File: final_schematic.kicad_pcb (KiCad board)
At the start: 2 copper layers, 54.7 x 60.6 mm, 56 parts, among them J1 Battery Babysitter, J2 BB_SYSOFF, J4 OLED Qwiic, J5 Programmer, J8 GPS_COAX, SW1 SW_Push_SESS, SW2 SW_Push_RADIO, SW3 SW_Push_RST, U1 STM32L476VGTx, U2 MTK3339, U3 RFM95W-868S2, U4 BNO055, U5 LT1129-3.3_SO8, U6 TC2014-3.3VxCTTR

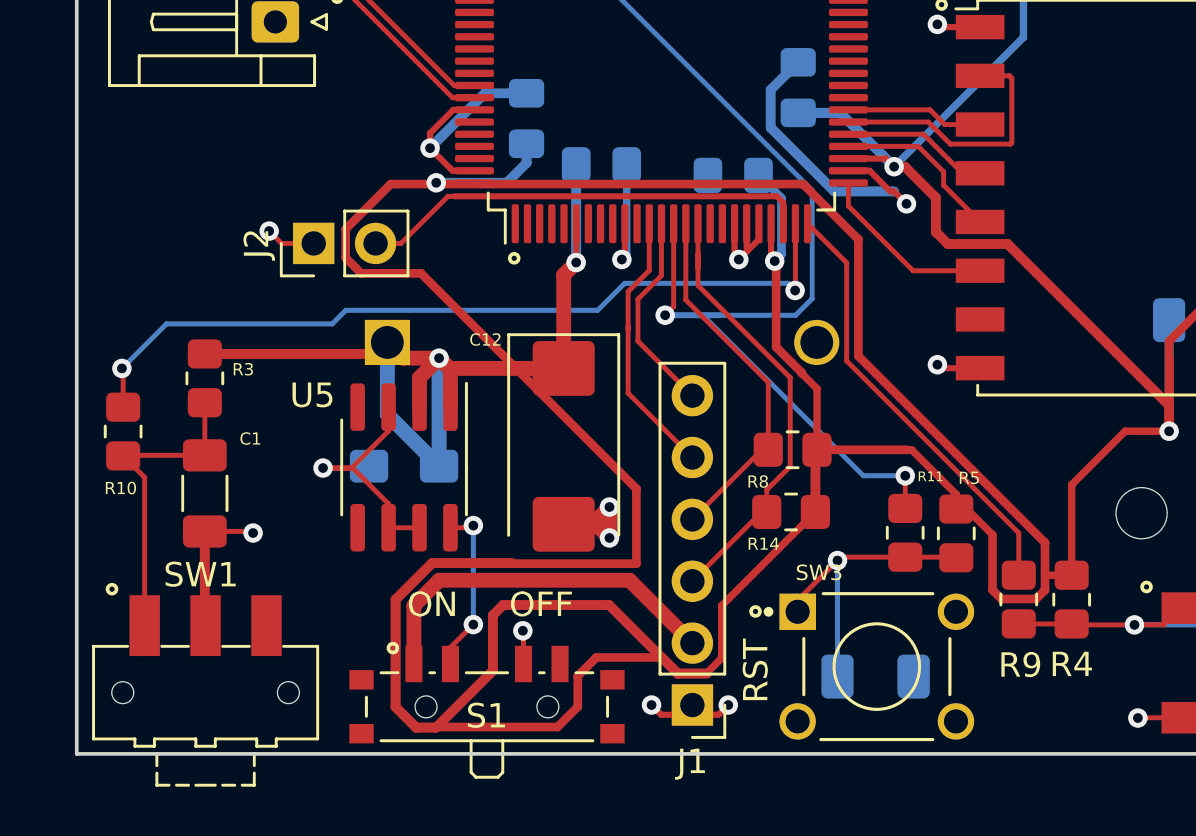
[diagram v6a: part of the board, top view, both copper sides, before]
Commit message: routing minimization
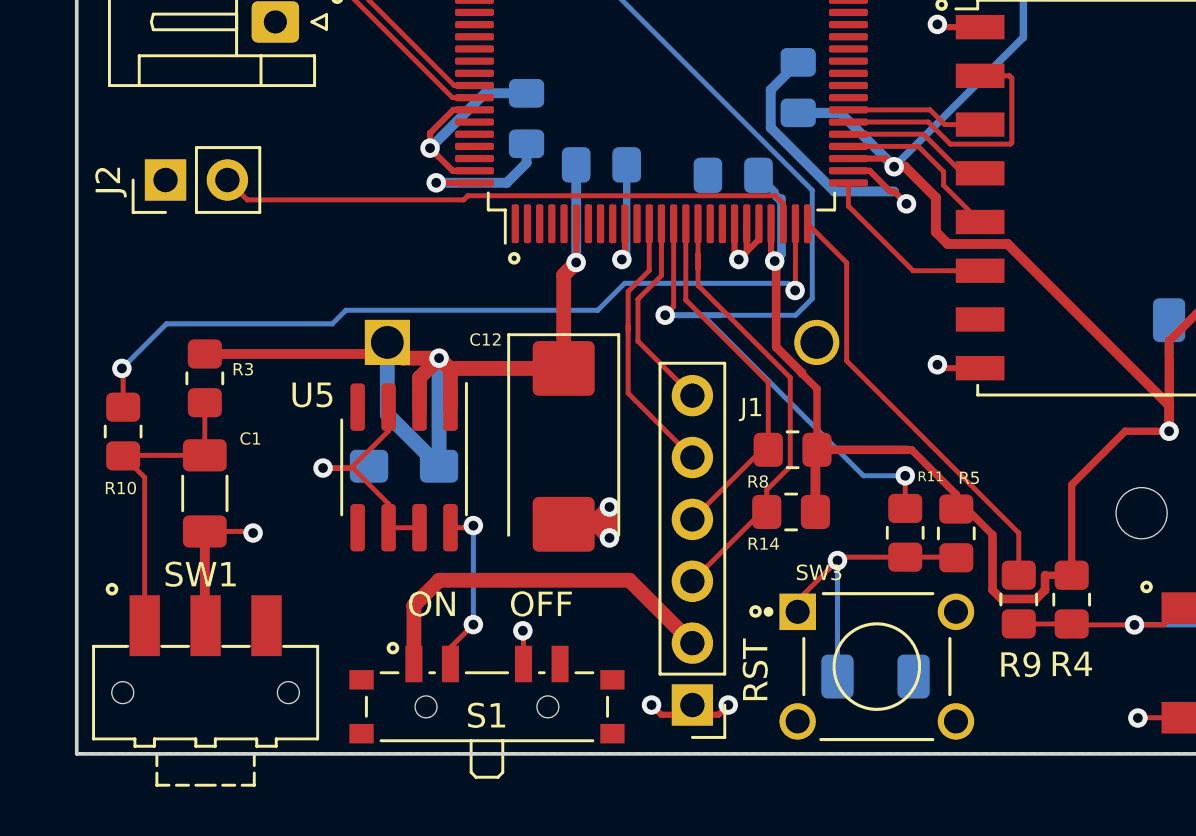
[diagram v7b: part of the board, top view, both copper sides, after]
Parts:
- moved J2 6.62 mm to (100.9, 82.3)
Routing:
- net 3V3: track 370.4 -> 244.5 mm
- net SYSOFF: track 18.5 -> 24.2 mm
- net GND: track 150.0 -> 148.0 mm, vias 27 -> 26
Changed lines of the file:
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@@
     (thickness 1.6)
     (drawings 51)
-    (tracks 612)
+    (tracks 573)
     (zones 0)
     (modules 56)
@@
   )
   (setup
-    (last_trace_width 0.254)
+    (last_trace_width 0.2032)
     (user_trace_width 0.2032)
     (user_trace_width 0.254)
@@
     )
   )
-  (module Connector_PinHeader_2.54mm:PinHeader_1x02_P2.54mm_Vertical (layer F.Cu)
-    (at 106.9848 84.9376 90)
+  (module Connector_PinHeader_2.54mm:PinHeader_1x02_P2.54mm_Vertical locked (layer F.Cu)
+    (at 100.9015 82.3341 90)
     (descr "Through hole straight pin header, 1x02, 2.54mm pitch, single row")
     (tags "Through hole pin header THT 1x02 2.54mm single row")
@@
     )
   )
-  (module Connector_PinHeader_2.54mm:PinHeader_1x06_P2.54mm_Vertical (layer F.Cu)
+  (module Connector_PinHeader_2.54mm:PinHeader_1x06_P2.54mm_Vertical locked (layer F.Cu)
     (at 122.5296 103.886 180)
     (descr "Through hole straight pin header, 1x06, 2.54mm pitch, single row")
     (tags "Through hole pin header THT 1x06 2.54mm single row")
-    (fp_text reference J1 (at 0 -2.33) (layer F.SilkS)
-      (effects (font (size 1 1) (thickness 0.15)))
+    (fp_text reference J1 (at -2.4384 12.2047) (layer F.SilkS)
+      (effects (font (size 0.75 0.75) (thickness 0.15)))
     )
     (fp_text value "Battery Babysitter" (at 0 15.03) (layer F.Fab)
@@
   (segment (start 130.468 70.954) (end 130.4925 70.9295) (width 0.254) (layer F.Cu) (net 2))
   (segment (start 128.9346 70.954) (end 130.468 70.954) (width 0.254) (layer F.Cu) (net 2))
-  (via (at 105.156 84.4296) (size 0.8) (drill 0.4) (layers F.Cu B.Cu) (net 2))
-  (segment (start 105.664 84.9376) (end 105.156 84.4296) (width 0.2032) (layer F.Cu) (net 2))
-  (segment (start 106.9848 84.9376) (end 105.664 84.9376) (width 0.2032) (layer F.Cu) (net 2))
   (segment (start 122.153494 103.4956) (end 122.5296 103.4956) (width 0.6096) (layer F.Cu) (net 2))
   (segment (start 107.556399 61.201399) (end 107.895224 61.201399) (width 0.2032) (layer F.Cu) (net 24))
@@
   (segment (start 127.5809 93.472) (end 127.6444 93.4085) (width 0.4064) (layer F.Cu) (net 5))
   (segment (start 127.5809 95.9612) (end 127.5809 93.472) (width 0.4064) (layer F.Cu) (net 5))
-  (segment (start 110.343599 99.558418) (end 111.845228 98.056789) (width 0.4064) (layer F.Cu) (net 5))
-  (segment (start 111.845228 98.056789) (end 115.125771 98.056789) (width 0.4064) (layer F.Cu) (net 5))
-  (segment (start 114.758865 99.780799) (end 114.341201 100.198463) (width 0.4064) (layer F.Cu) (net 5))
-  (segment (start 112.006337 104.815201) (end 111.187263 104.815201) (width 0.4064) (layer F.Cu) (net 5))
-  (segment (start 123.131137 102.599201) (end 121.928063 102.599201) (width 0.4064) (layer F.Cu) (net 5))
-  (segment (start 121.928063 102.599201) (end 119.109661 99.780799) (width 0.4064) (layer F.Cu) (net 5))
-  (segment (start 114.341201 100.198463) (end 114.341201 102.480337) (width 0.4064) (layer F.Cu) (net 5))
-  (segment (start 110.343599 103.971537) (end 110.343599 99.558418) (width 0.4064) (layer F.Cu) (net 5))
-  (segment (start 114.341201 102.480337) (end 112.006337 104.815201) (width 0.4064) (layer F.Cu) (net 5))
-  (segment (start 119.109661 99.780799) (end 114.758865 99.780799) (width 0.4064) (layer F.Cu) (net 5))
-  (segment (start 111.187263 104.815201) (end 110.343599 103.971537) (width 0.4064) (layer F.Cu) (net 5))
-  (segment (start 121.940255 102.573801) (end 123.118945 102.573801) (width 0.3556) (layer F.Cu) (net 5))
-  (segment (start 121.301799 101.935345) (end 121.940255 102.573801) (width 0.3556) (layer F.Cu) (net 5))
-  (segment (start 118.583413 101.935345) (end 121.301799 101.935345) (width 0.3556) (layer F.Cu) (net 5))
-  (segment (start 117.824601 102.694157) (end 118.583413 101.935345) (width 0.3556) (layer F.Cu) (net 5))
-  (segment (start 117.824601 103.959345) (end 117.824601 102.694157) (width 0.3556) (layer F.Cu) (net 5))
-  (segment (start 116.994145 104.789801) (end 117.824601 103.959345) (width 0.3556) (layer F.Cu) (net 5))
-  (segment (start 111.199455 104.789801) (end 116.994145 104.789801) (width 0.3556) (layer F.Cu) (net 5))
-  (segment (start 110.368999 103.959345) (end 111.199455 104.789801) (width 0.3556) (layer F.Cu) (net 5))
-  (segment (start 110.368999 99.568939) (end 110.368999 103.959345) (width 0.3556) (layer F.Cu) (net 5))
-  (segment (start 111.855748 98.08219) (end 110.368999 99.568939) (width 0.3556) (layer F.Cu) (net 5))
-  (segment (start 120.231145 98.082189) (end 111.855748 98.08219) (width 0.3556) (layer F.Cu) (net 5))
-  (segment (start 120.231145 95.005489) (end 120.231145 98.082189) (width 0.3556) (layer F.Cu) (net 5))
-  (segment (start 111.391057 86.165401) (end 120.231145 95.005489) (width 0.3556) (layer F.Cu) (net 5))
-  (segment (start 108.935455 86.165401) (end 111.391057 86.165401) (width 0.3556) (layer F.Cu) (net 5))
-  (segment (start 108.296999 85.526945) (end 108.935455 86.165401) (width 0.3556) (layer F.Cu) (net 5))
-  (segment (start 108.296999 84.348255) (end 108.296999 85.526945) (width 0.3556) (layer F.Cu) (net 5))
-  (segment (start 110.144074 82.50118) (end 108.296999 84.348255) (width 0.3556) (layer F.Cu) (net 5))
-  (segment (start 127.072152 82.50118) (end 110.144074 82.50118) (width 0.3556) (layer F.Cu) (net 5))
-  (segment (start 129.343111 84.772139) (end 127.072152 82.50118) (width 0.3556) (layer F.Cu) (net 5))
-  (segment (start 129.343111 89.563125) (end 129.343111 84.772139) (width 0.3556) (layer F.Cu) (net 5))
-  (segment (start 137.00591 97.225924) (end 129.343111 89.563125) (width 0.3556) (layer F.Cu) (net 5))
   (segment (start 136.63815 99.53311) (end 137.00591 99.16535) (width 0.3556) (layer F.Cu) (net 5))
   (segment (start 135.21805 99.53311) (end 136.63815 99.53311) (width 0.3556) (layer F.Cu) (net 5))
@@
   (segment (start 127.6444 90.903262) (end 127.6444 93.4085) (width 0.3048) (layer F.Cu) (net 5))
   (segment (start 127.025419 90.284281) (end 127.6444 90.903262) (width 0.3048) (layer F.Cu) (net 5))
-  (segment (start 123.732001 99.810099) (end 127.5809 95.9612) (width 0.3048) (layer F.Cu) (net 5))
-  (segment (start 123.732001 101.960745) (end 123.732001 99.810099) (width 0.3048) (layer F.Cu) (net 5))
-  (segment (start 123.118945 102.573801) (end 123.732001 101.960745) (width 0.3048) (layer F.Cu) (net 5))
   (segment (start 133.795652 95.8408) (end 134.85029 96.895438) (width 0.3048) (layer F.Cu) (net 5))
   (segment (start 133.3627 95.8408) (end 133.795652 95.8408) (width 0.3048) (layer F.Cu) (net 5))
@@
   (segment (start 137.0142 98.5586) (end 137.00591 98.55031) (width 0.3048) (layer F.Cu) (net 5))
   (segment (start 138.0998 98.5586) (end 137.0142 98.5586) (width 0.3048) (layer F.Cu) (net 5))
-  (segment (start 137.00591 98.55031) (end 137.00591 97.225924) (width 0.3556) (layer F.Cu) (net 5))
   (segment (start 137.00591 99.16535) (end 137.00591 98.55031) (width 0.3556) (layer F.Cu) (net 5))
   (segment (start 143.3296 67.0586) (end 143.5608 66.8274) (width 0.254) (layer F.Cu) (net 5))
@@
   (segment (start 136.1186 73.7837) (end 136.1186 76.4794) (width 0.3048) (layer B.Cu) (net 5))
   (segment (start 125.9332 82.8333) (end 125.2435 82.1436) (width 0.3048) (layer B.Cu) (net 5))
-  (segment (start 126.1872 83.0873) (end 125.9332 82.8333) (width 0.3556) (layer B.Cu) (net 5))
+  (segment (start 126.1364 83.1635) (end 125.8824 82.9095) (width 0.3556) (layer B.Cu) (net 5))
   (segment (start 127.025419 90.249759) (end 127.025419 90.284281) (width 0.3556) (layer F.Cu) (net 5))
   (segment (start 125.968199 89.192539) (end 127.025419 90.249759) (width 0.3556) (layer F.Cu) (net 5))
@@
   (segment (start 120.2944 88.9508) (end 120.2944 87.2236) (width 0.2032) (layer F.Cu) (net 14))
   (segment (start 122.5296 91.186) (end 120.2944 88.9508) (width 0.2032) (layer F.Cu) (net 14))
-  (segment (start 126.000292 83.00399) (end 126.2596 83.263298) (width 0.25) (layer F.Cu) (net 15))
-  (segment (start 126.2596 83.263298) (end 126.2596 84.129) (width 0.25) (layer F.Cu) (net 15))
-  (segment (start 112.768888 83.00399) (end 126.000292 83.00399) (width 0.25) (layer F.Cu) (net 15))
-  (segment (start 110.56317 84.9376) (end 109.5248 84.9376) (width 0.2032) (layer F.Cu) (net 15))
-  (segment (start 112.49678 83.00399) (end 110.56317 84.9376) (width 0.2032) (layer F.Cu) (net 15))
-  (segment (start 112.768888 83.00399) (end 112.49678 83.00399) (width 0.2032) (layer F.Cu) (net 15))
+  (segment (start 125.9438 82.98059) (end 113.31061 82.98059) (width 0.2032) (layer F.Cu) (net 15))
+  (segment (start 126.2596 83.29639) (end 125.9438 82.98059) (width 0.2032) (layer F.Cu) (net 15))
+  (segment (start 126.2596 84.129) (end 126.2596 83.29639) (width 0.2032) (layer F.Cu) (net 15))
+  (segment (start 104.257401 83.150001) (end 103.4415 82.3341) (width 0.2032) (layer F.Cu) (net 15))
+  (segment (start 113.141199 83.150001) (end 104.257401 83.150001) (width 0.2032) (layer F.Cu) (net 15))
+  (segment (start 113.31061 82.98059) (end 113.141199 83.150001) (width 0.2032) (layer F.Cu) (net 15))
   (segment (start 112.681765 78.954) (end 113.5846 78.954) (width 0.2032) (layer F.Cu) (net 16))
   (segment (start 108.347 74.619235) (end 112.681765 78.954) (width 0.2032) (layer F.Cu) (net 16))

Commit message: routing minimization peer review
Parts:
- moved R4 0.17 mm to (138.3, 99.6)
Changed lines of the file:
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@@
     (thickness 1.6)
     (drawings 51)
-    (tracks 573)
+    (tracks 572)
     (zones 0)
     (modules 56)
@@
   )
   (module Resistor_SMD:R_0805_2012Metric_Pad1.20x1.40mm_HandSolder (layer F.Cu)
-    (at 138.0998 99.5586 270)
+    (at 138.2649 99.5586 270)
     (descr "Resistor SMD 0805 (2012 Metric), square (rectangular) end terminal, IPC_7351 nominal with elongated pad for handsoldering. (Body size source: IPC-SM-782 page 72, https://www.pcb-3d.com/wordpress/wp-content/uploads/ipc-sm-782a_amendment_1_and_2.pdf), generated with kicad-footprint-generator")
     (tags "resistor handsolder")
@@
   (segment (start 140.6536 100.5724) (end 140.6775 100.5963) (width 0.2032) (layer F.Cu) (net 3))
   (segment (start 138.1375 100.5963) (end 138.0998 100.5586) (width 0.2032) (layer F.Cu) (net 3))
-  (segment (start 140.6775 100.5963) (end 138.1375 100.5963) (width 0.2032) (layer F.Cu) (net 3))
   (segment (start 135.9314 100.5586) (end 135.9281 100.5553) (width 0.2032) (layer F.Cu) (net 3))
   (segment (start 138.0998 100.5586) (end 135.9314 100.5586) (width 0.2032) (layer F.Cu) (net 3))
+  (segment (start 140.6398 100.5586) (end 140.6775 100.5963) (width 0.2032) (layer F.Cu) (net 3))
+  (segment (start 138.2649 100.5586) (end 140.6398 100.5586) (width 0.2032) (layer F.Cu) (net 3))
   (segment (start 128.4855 97.9547) (end 128.4855 97.9547) (width 0.25) (layer B.Cu) (net 4))
   (via (at 128.4855 97.9547) (size 0.8) (drill 0.4) (layers F.Cu B.Cu) (net 4))
@@
   (segment (start 111.6584 70.1929) (end 111.9251 70.1929) (width 0.6096) (layer B.Cu) (net 5))
   (segment (start 142.0999 92.6469) (end 140.2965 92.6469) (width 0.3048) (layer F.Cu) (net 5))
-  (segment (start 138.0998 94.8436) (end 138.0998 98.5586) (width 0.3048) (layer F.Cu) (net 5))
   (segment (start 140.2965 92.6469) (end 138.0998 94.8436) (width 0.3048) (layer F.Cu) (net 5))
   (segment (start 127.5809 93.472) (end 127.6444 93.4085) (width 0.4064) (layer F.Cu) (net 5))
   (segment (start 127.5809 95.9612) (end 127.5809 93.472) (width 0.4064) (layer F.Cu) (net 5))
-  (segment (start 136.63815 99.53311) (end 137.00591 99.16535) (width 0.3556) (layer F.Cu) (net 5))
-  (segment (start 135.21805 99.53311) (end 136.63815 99.53311) (width 0.3556) (layer F.Cu) (net 5))
-  (segment (start 134.85029 99.16535) (end 135.21805 99.53311) (width 0.3556) (layer F.Cu) (net 5))
-  (segment (start 134.85029 96.895438) (end 134.85029 99.16535) (width 0.3556) (layer F.Cu) (net 5))
   (segment (start 127.6444 93.4085) (end 131.363352 93.4085) (width 0.3556) (layer F.Cu) (net 5))
   (segment (start 127.6444 90.903262) (end 127.6444 93.4085) (width 0.3048) (layer F.Cu) (net 5))
@@
   (segment (start 133.3627 95.2408) (end 131.5304 93.4085) (width 0.3048) (layer F.Cu) (net 5))
   (segment (start 133.3627 95.8408) (end 133.3627 95.2408) (width 0.3048) (layer F.Cu) (net 5))
-  (segment (start 137.0142 98.5586) (end 137.00591 98.55031) (width 0.3048) (layer F.Cu) (net 5))
-  (segment (start 138.0998 98.5586) (end 137.0142 98.5586) (width 0.3048) (layer F.Cu) (net 5))
-  (segment (start 137.00591 99.16535) (end 137.00591 98.55031) (width 0.3556) (layer F.Cu) (net 5))
   (segment (start 143.3296 67.0586) (end 143.5608 66.8274) (width 0.254) (layer F.Cu) (net 5))
   (segment (start 142.0991 67.0586) (end 143.3296 67.0586) (width 0.254) (layer F.Cu) (net 5))
@@
   (segment (start 125.7596 85.5133) (end 125.9078 85.6615) (width 0.254) (layer F.Cu) (net 5))
   (segment (start 125.7596 84.129) (end 125.7596 85.5133) (width 0.254) (layer F.Cu) (net 5))
+  (segment (start 137.29039 99.53311) (end 138.2649 98.5586) (width 0.3556) (layer F.Cu) (net 5))
+  (segment (start 134.85029 99.16535) (end 135.21805 99.53311) (width 0.3556) (layer F.Cu) (net 5))
+  (segment (start 135.21805 99.53311) (end 137.29039 99.53311) (width 0.3556) (layer F.Cu) (net 5))
+  (segment (start 134.85029 96.895438) (end 134.85029 99.16535) (width 0.3556) (layer F.Cu) (net 5))
+  (segment (start 138.0998 98.3935) (end 138.2649 98.5586) (width 0.3048) (layer F.Cu) (net 5))
+  (segment (start 138.0998 94.8436) (end 138.0998 98.3935) (width 0.3048) (layer F.Cu) (net 5))
   (segment (start 135.9567 68.0586) (end 135.89 67.9919) (width 0.2032) (layer F.Cu) (net 6))
   (segment (start 138.7741 68.0586) (end 135.9567 68.0586) (width 0.2032) (layer F.Cu) (net 6))
